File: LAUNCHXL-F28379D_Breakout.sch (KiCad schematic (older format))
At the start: 28 parts, among them Q1 100V/17A, Q2 100V/17A, Q3 100V/17A, Q4 100V/17A, Q5 100V/17A, Q6 100V/17A, U2 TL084CN, U5 STK681-332-E

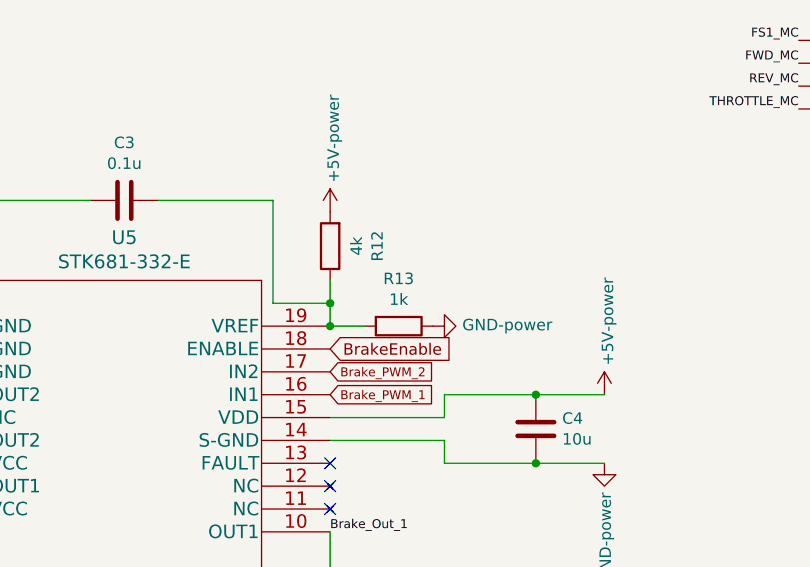
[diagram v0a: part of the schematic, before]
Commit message: updated motor driver connections
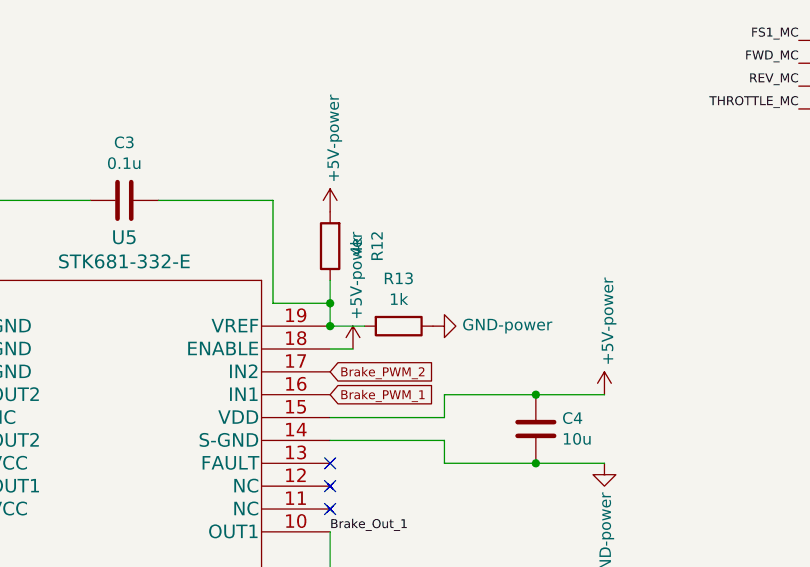
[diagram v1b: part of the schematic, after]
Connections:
- net BrakeEnable is gone; now on net +5V: U5.18 (ENABLE)
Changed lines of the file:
@@
 	0    -1   -1   0
 $EndComp
-Text GLabel 8900 5700 2    50   Input ~ 0
-BrakeEnable
 $Comp
 L PCB_2020-rescue:C-Device C4
@@
 NoConn ~ 8900 6300
 NoConn ~ 8900 6400
+$Comp
+L PCB_2020-rescue:+5V-power #PWR?
+U 1 1 61745E44
+P 9000 5700
+F 0 "#PWR?" H 9000 5550 50  0001 C CNN
+F 1 "+5V-power" V 9015 5828 50  0000 L CNN
+F 2 "" H 9000 5700 50  0001 C CNN
+F 3 "" H 9000 5700 50  0001 C CNN
+	1    9000 5700
+	1    0    0    -1
+$EndComp
+Wire Wire Line
+	8900 5700 9000 5700
 $EndSCHEMATC
